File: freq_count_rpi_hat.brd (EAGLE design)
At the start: 65 x 56 mm, 32 parts, among them IC1 LTC6752, IC2 LTC6752, P1 47k, U1 SN74LV8154PW, U2 SN74LV8154PW, X1 RASPI_BOARD_B+#_HD

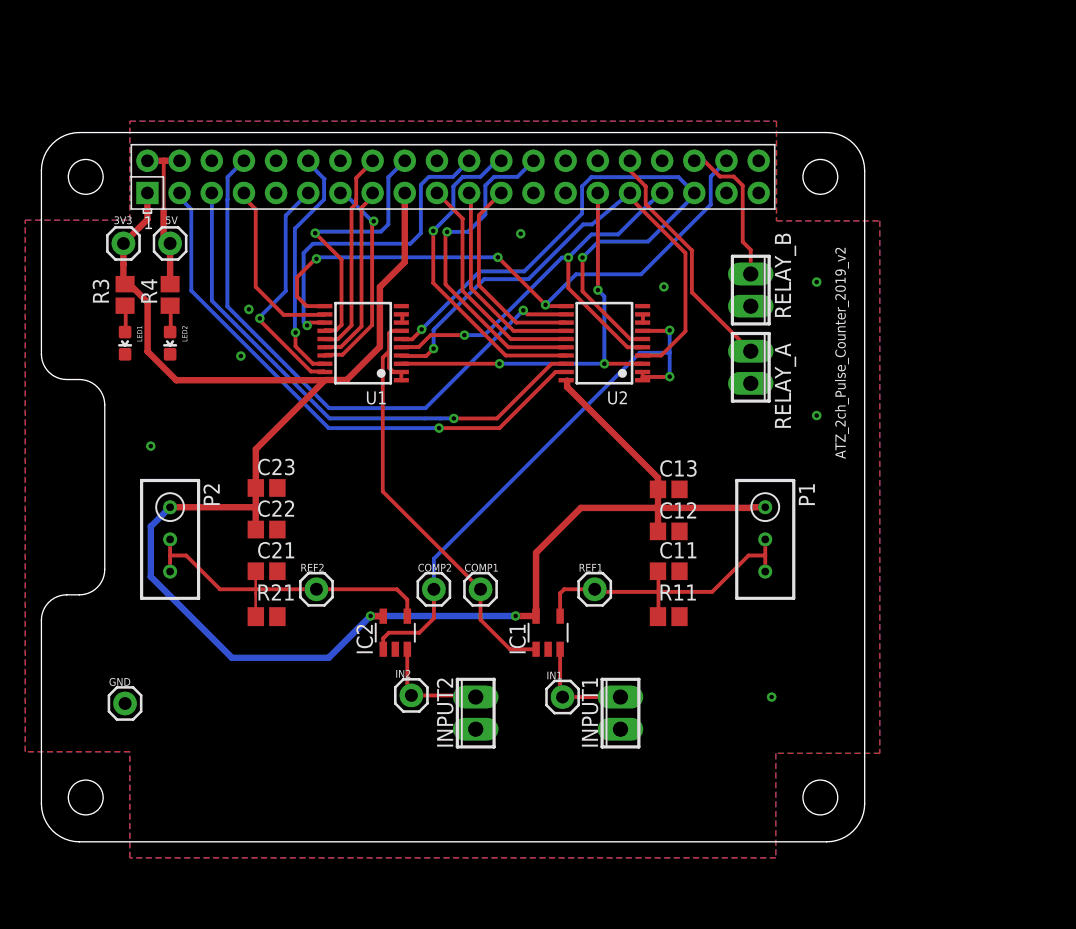
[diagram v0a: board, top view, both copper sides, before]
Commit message: Updated with mode selection switches and mistakes in design were corrected
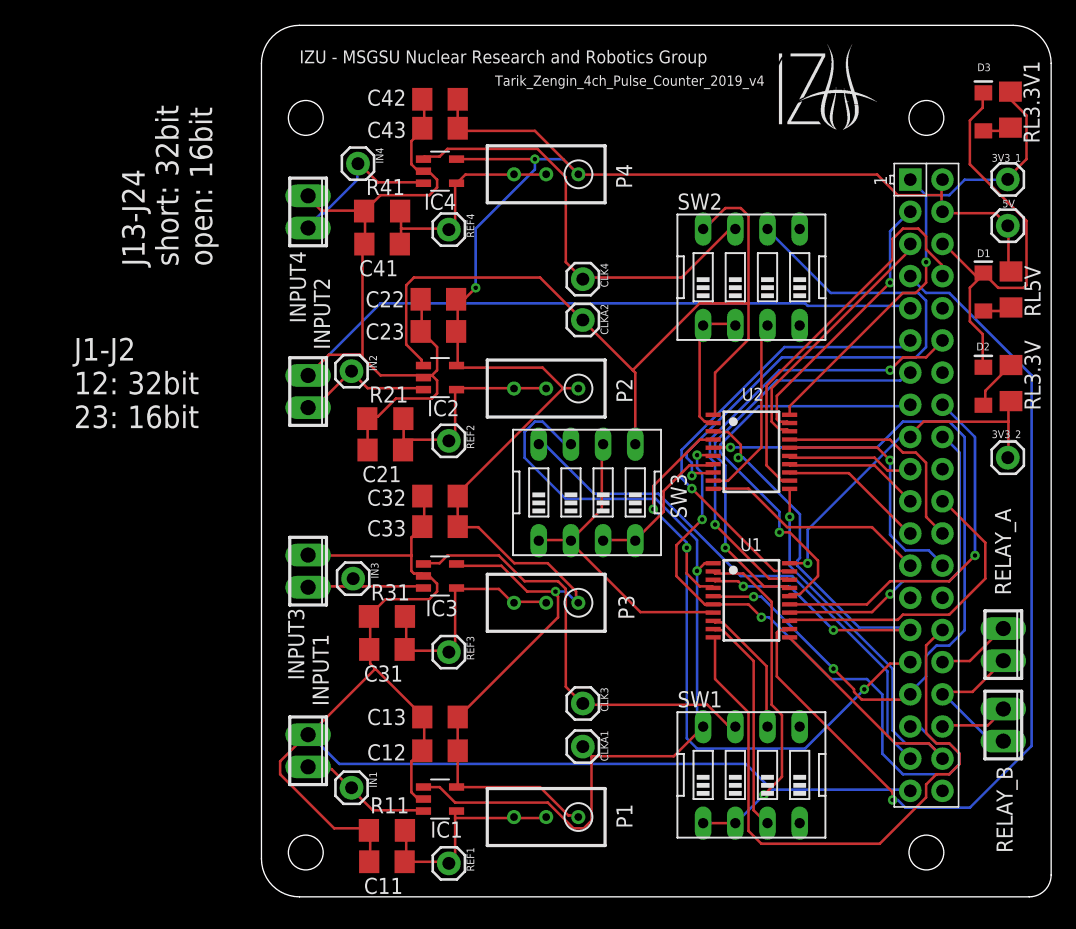
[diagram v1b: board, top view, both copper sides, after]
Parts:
- removed 3V3, COMP1, COMP2, GND: (no value), SparkFun-Connectors:1X01
- removed LED1, LED2: Rled, BeagleBone_Blue_R3:0603-RED
- removed R3, R4: RESISTOR0805, BeagleBone_Blue_R3:R0805
- added 3V3_1, 3V3_2, CLK3, CLK4, CLKA1, CLKA2, IN3, IN4, REF3, REF4: (no value), SparkFun-Connectors:1X01
- added C31, C32, C33, C41, C42, C43: (no value), resistor:C1206
- added D1, D2, D3: (no value), SparkFun-LED:LED-1206
- added IC3, IC4: LTC6752, linear:SOT23-5
- added INPUT3, INPUT4: (no value), con-phoenix-254:2POL254
- added P3: 47k, rcl:RTRIM3296W
- added P4: (no value), rcl:RTRIM3296W
- added R31, R41, RL3.3V, RL3.3V1, RL5V: (no value), resistor:R1206
- added SW1, SW2, SW3: (no value), special:EDG-04
- C11, C12, C13, C21, C22, C23: value CAPACITOR-N0805 -> (none); device BeagleBone_Blue_R3:C0805 -> resistor:C1206
- R11: value 470R -> (none); device BeagleBone_Blue_R3:R0805 -> resistor:R1206
- R21: value RESISTOR0805 -> (none); device BeagleBone_Blue_R3:R0805 -> resistor:R1206
- X1: value RASPI_BOARD_B+#_HD -> RASPI_BOARD_B+#_H; device raspberrypi_bastelstube_v13:RASPI_BOARD_B+HAT_DF -> raspberrypi_bastelstube_v13:RASPI_BOARD_B+HAT
- moved 5V 66.2 mm to (82.6, 52.5), turned to 270 degrees
- moved X1 63.1 mm to (23.7, 64.5), turned to 270 degrees
- moved RELAY_B 39.7 mm to (82.3, 13.0)
- moved U1 36.8 mm to (62.4, 22.9), turned to 270 degrees
- moved P2 32.0 mm to (46.2, 39.6), turned to 90 degrees
- moved C11 32.0 mm to (33.6, 2.24), turned to 180 degrees
- moved RELAY_A 29.6 mm to (82.3, 19.4)
- moved INPUT2 28.6 mm to (27.4, 39.4), turned to 270 degrees
- moved R11 27.9 mm to (33.6, 4.71), turned to 0 degrees
- moved P1 27.9 mm to (46.2, 5.77), turned to 90 degrees
- moved IN2 26.0 mm to (30.8, 41.0), turned to 270 degrees
- moved C13 25.5 mm to (37.8, 13.7), turned to 180 degrees
- moved C12 25.0 mm to (37.8, 11.0), turned to 180 degrees
- moved INPUT1 24.8 mm to (27.4, 11.0), turned to 270 degrees
- moved REF1 24.5 mm to (38.5, 2.11), turned to 270 degrees
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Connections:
- removed net 3.3V: 3V3.1, C12.1, C13.1, C22.1, C23.1, IC1.5, IC2.5, P1.1, P2.1, R3.2, U1.20, U2.20, X1.1, X1.17
- removed net CLK1: COMP1.1, IC1.1, U1.1, U1.2, U1.7
- removed net CLK2: COMP2.1, IC2.1, U2.1, U2.2, U2.7
- removed net GND: C11.2, C12.2, C13.2, C21.2, C22.2, C23.2, GND.1, IC1.2, IC2.2, INPUT1.1, INPUT2.1, LED1.C, LED2.C, R11.1, R21.1, RELAY_A.2, RELAY_B.2, U1.10, U2.10, X1.14, X1.20, X1.25, X1.30, X1.34, X1.39, X1.6, X1.9
- removed net N$21: U1.8, U1.9
- removed net N$22: U2.8, U2.9
- new net CLK3: CLK3.1, IC3.1, SW1.7
- new net CLK4: CLK4.1, IC4.1, SW2.7
- new net CLKA1: CLKA1.1, IC1.1, SW1.8, SW3.7, U1.1
- new net CLKA2: CLKA2.1, IC2.1, SW2.8, SW3.5, U2.1
- new net CLKB1: SW1.1, SW1.2, U1.2
- new net CLKB2: SW2.1, SW2.2, U2.2
- new net GNDA: D1.C, D2.C, D3.C, X1.6
- new net GNDB: C21.2, C22.2, C23.2, C41.2, C42.2, C43.2, IC2.2, IC4.2, INPUT2.1, INPUT4.1, R21.1, R41.1, X1.9
- new net GNDC: X1.14
- new net GNDD: X1.20
- new net GNDE: U2.10, X1.25
- new net GNDF: U1.10, X1.30
- new net GNDG: RELAY_A.2, RELAY_B.2, X1.34
- new net GNDH: C11.2, C12.2, C13.2, C31.2, C32.2, C33.2, IC1.2, IC3.2, INPUT1.1, INPUT3.1, R11.1, R31.1, X1.39
- new net IN3+: IC3.3, IN3.1, INPUT3.2
- new net IN4+: IC4.3, IN4.1, INPUT4.2
- new net J13_CLKEN1: SW1.3, U1.9
- new net J13_CLKEN2: SW1.6, U1.8
- new net J24_CLKEN1: SW2.3, U2.9
- new net J24_CLKEN2: SW2.6, U2.8
- new net N$11: SW1.5
- new net N$3: D3.A, RL3.3V1.1
- new net N$4: SW1.4
- new net N$5: SW2.4
- new net N$9: SW2.5
- new net RCLK1: SW3.1, SW3.2, SW3.6, U1.7
- new net RCLK2: SW3.3, SW3.4, U2.7
- new net RCLK_CNTL: SW3.8, X1.37
- new net REF3: C31.1, IC3.4, P3.2, P3.3, R31.2, REF3.1
- new net REF4: C41.1, IC4.4, P4.2, P4.3, R41.2, REF4.1
- new net VCC_1: 3V3_1.1, RL3.3V1.2, U2.20, X1.1
- new net VCC_2: 3V3_2.1, RL3.3V.2, U1.20, X1.17
- net 5V: now also C12.1, C13.1, C22.1, C23.1, C32.1, C33.1, C42.1, C43.1, IC1.5, IC2.5, IC3.5, IC4.5, P1.1, P2.1, P3.1, P4.1, RL5V.2; no longer R4.2
- net N$1: now also D1.A, RL5V.1; no longer LED2.A, R4.1
- net N$2: now also D2.A, RL3.3V.1; no longer LED1.A, R3.1
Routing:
- net 3.3V: track 149.8 -> 0.00 mm, vias 2 -> 0
- net 5V: track 12.5 -> 161.9 mm, vias 0 -> 3
- net GNDH: track 0.00 -> 114.0 mm
- net GNDB: track 0.00 -> 110.8 mm
- net CLKA1: track 0.00 -> 70.4 mm, vias 0 -> 1
- net CLKA2: track 0.00 -> 66.8 mm
- net CNT1_Y7: track 14.2 -> 73.5 mm, vias 0 -> 1
- net GNDF: track 0.00 -> 49.6 mm
- net J24_CLKEN2: track 0.00 -> 44.7 mm, vias 0 -> 1
- net CLK2: track 44.3 -> 0.00 mm, vias 2 -> 0
- net RCLK_CNTL: track 0.00 -> 42.6 mm
- net VCC_1: track 0.00 -> 39.2 mm, vias 0 -> 1
- net CLK1: track 35.5 -> 0.00 mm
- net CLK3: track 0.00 -> 35.0 mm
- net CLK4: track 0.00 -> 34.9 mm
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- removed copper zone on layer 1, net GND
- removed copper zone on layer 16, net GND
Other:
- board size 65 x 56 mm -> 62.3 x 68.8 mm
- board text added: "IZU - MSGSU Nuclear Research and Robotics Group"
- board text added: "J1-J2 12: 32bit 23: 16bit"
- board text added: "J13-J24 short: 32bit open: 16bit"
- board text added: "Tarik_Zengin_4ch_Pulse_Counter_2019_v4"
- board text removed: "ATZ_2ch_Pulse_Counter_2019_v2"
